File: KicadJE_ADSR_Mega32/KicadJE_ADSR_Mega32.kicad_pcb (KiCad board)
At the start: 2 copper layers, 100 x 100 mm, 126 parts, among them J101 ADSR1, J102 ADSR2, J103 ADSR1, J104 ADSR2, J105 ADSR1-G8, J106 ADSR2-G8, J107 ADSR4-G8, J108 ADSR3-G8, J201 AVR-ISP-6, J202 UART, J301 In, J302 +5V reg/doepfer, J303 Out, J304 CV_time, J305 CV doepfer, P101 Doepfer_Power_16pin, P302 Doepfer_Power_16pin, Q301 BC337, Q302 PZT2222A, U201 ATmega32A-AU, U301 L78L05_TO92, U302 PT2399, Y201 16MHz

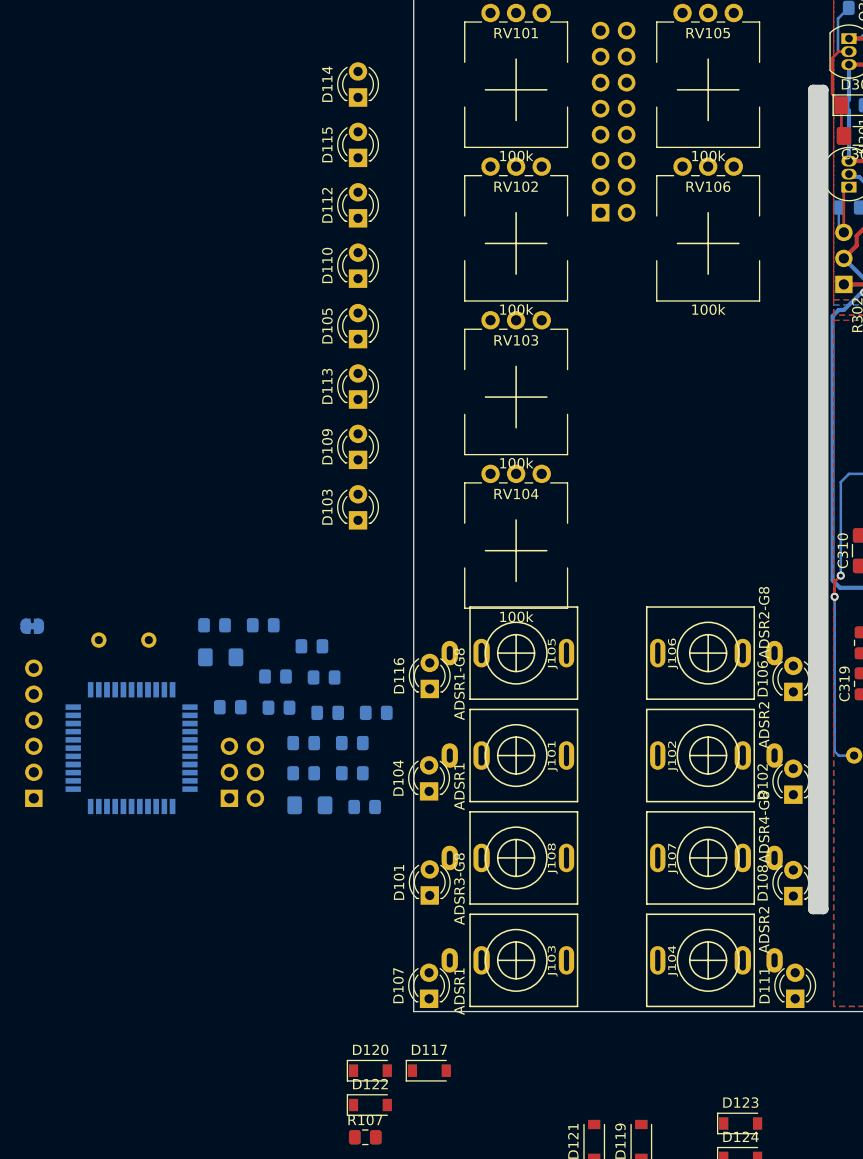
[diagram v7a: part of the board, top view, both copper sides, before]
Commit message: Fix LED matrix
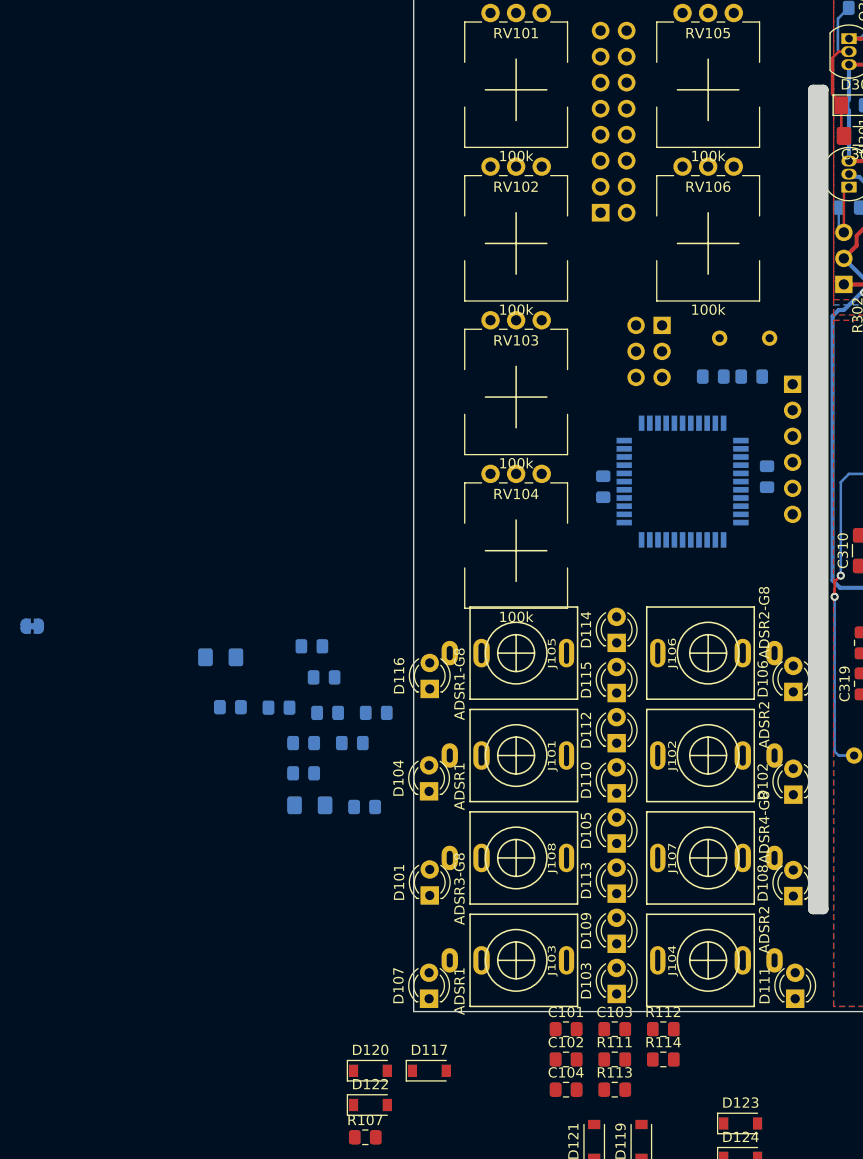
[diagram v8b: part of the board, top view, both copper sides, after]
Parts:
- added C101: 100n, Capacitor_SMD:C_0805_2012Metric_Pad1.15x1.40mm_HandSolder, F.Cu at (64.9, 151.7)
- added C102: 1u, Capacitor_SMD:C_0805_2012Metric_Pad1.15x1.40mm_HandSolder, F.Cu at (64.9, 154.7)
- added C103: 100n, Capacitor_SMD:C_0805_2012Metric_Pad1.15x1.40mm_HandSolder, F.Cu at (69.6, 151.7)
- added C104: 1u, Capacitor_SMD:C_0805_2012Metric_Pad1.15x1.40mm_HandSolder, F.Cu at (64.9, 157.6)
- added R111: 1k, Resistor_SMD:R_0805_2012Metric_Pad1.15x1.40mm_HandSolder, F.Cu at (69.6, 154.7)
- added R112: 10k, Resistor_SMD:R_0805_2012Metric_Pad1.15x1.40mm_HandSolder, F.Cu at (74.4, 151.7)
- added R113: 1k, Resistor_SMD:R_0805_2012Metric_Pad1.15x1.40mm_HandSolder, F.Cu at (69.6, 157.6)
- added R114: 10k, Resistor_SMD:R_0805_2012Metric_Pad1.15x1.40mm_HandSolder, F.Cu at (74.4, 154.7)
- moved J202 84.4 mm to (87.0, 88.8), turned to 180 degrees
- moved Y201 71.8 mm to (84.8, 84.2), turned to 180 degrees
- moved J201 62.6 mm to (74.2, 83.0), turned to 180 degrees
- moved U201 59.8 mm to (76.2, 98.2), turned to 270 degrees
- moved D114 58.9 mm to (69.8, 114.0)
- moved D115 58.0 mm to (69.8, 118.9)
- moved D112 57.1 mm to (69.8, 123.8)
- moved D110 56.2 mm to (69.8, 128.7)
- moved D105 55.3 mm to (69.8, 133.6)
- moved C209 54.9 mm to (83.0, 88.0), turned to 180 degrees
- moved D113 54.5 mm to (69.8, 138.5)
- moved D109 53.6 mm to (69.8, 143.4)
- moved D103 52.7 mm to (69.8, 148.3)
- moved C210 52.4 mm to (79.2, 88.0)
- moved C201 51.3 mm to (84.5, 97.8), turned to 90 degrees
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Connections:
- D102 pad 2: 0_LED -> 18
- D103 pad 2: 0_LED -> 18
- D104 pad 2: 0_LED -> 18
- D106 pad 2: 1 -> 19
- D107 pad 2: 1 -> 19
- D108 pad 2: 1 -> 19
- D110 pad 2: 2_INT2 -> 20
- D111 pad 2: 2_INT2 -> 20
- D112 pad 2: 2_INT2 -> 20
- D114 pad 2: 3_PWM -> 21
- D115 pad 2: 3_PWM -> 21
- D116 pad 2: 3_PWM -> 21
- D123 pad 2: ADSR1 -> ADSR4-G8
- D124 pad 1: ADSR1 -> ADSR4-G8
- J102 pad T: 4_PWM -> ADSR2
- J103 pad T: 12_PWM -> ADSR3
- J104 pad T: 13_PWM -> ADSR4
- J107 pad T: (no net) -> ADSR4-G8
- R108 pad 2: ADSR1 -> ADSR4-G8
- U201 pad 15: (no net) -> 14_PWM
- U201 pad 16: (no net) -> 15_PWM
- U201 pad 44: 4_PWM -> (no net)
